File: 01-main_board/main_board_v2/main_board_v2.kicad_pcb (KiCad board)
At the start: 4 copper layers, 96.4 x 65.3 mm, 3 parts, among them J1 Mezzanine Edge, J4 DB44 (Analog | Digital)

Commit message: made progress on layout
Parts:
- added AE1: Antenna_Chip, 22XT_Main:XDCR_2450AT18B100E, F.Cu at (111.2, 143.1)
- added BT1: Battery_Cell, Battery:BatteryHolder_LINX_BAT-HLD-012-SMT, F.Cu at (109.0, 76.5)
- added C1: 1 uF, Capacitor_SMD:C_0402_1005Metric, B.Cu at (99.5, 49.0)
- added C10: 4.7uF, Capacitor_SMD:C_0402_1005Metric, B.Cu at (72.1, 46.4)
- added C11: 10uF, Capacitor_SMD:C_0402_1005Metric, F.Cu at (206.3, 106.7)
- added C12: 0.1uF, Capacitor_SMD:C_0402_1005Metric, F.Cu at (206.3, 108.7)
- added C13: 1uF, Capacitor_SMD:C_0402_1005Metric, F.Cu at (151.5, 162.0)
- added C14: 0.1uF, Capacitor_SMD:C_0402_1005Metric, F.Cu at (151.5, 164.0)
- added C15: 10uF, Capacitor_SMD:C_0402_1005Metric, F.Cu at (151.5, 166.0)
- added C16: 0.1uF, Capacitor_SMD:C_0402_1005Metric, F.Cu at (151.5, 167.9)
- added C17: 0.1uF, Capacitor_SMD:C_0402_1005Metric, F.Cu at (151.5, 169.9)
- added C18: 0.1uF, Capacitor_SMD:C_0402_1005Metric, F.Cu at (151.5, 171.9)
- added C19: 1uF, Capacitor_SMD:C_0402_1005Metric, F.Cu at (151.5, 173.8)
- added C2: 1 uF, Capacitor_SMD:C_0402_1005Metric, B.Cu at (106.0, 49.9)
- added C20: 0.1uF, Capacitor_SMD:C_0402_1005Metric, F.Cu at (154.3, 162.0)
- added C21: 0.1uF, Capacitor_SMD:C_0402_1005Metric, F.Cu at (182.7, 80.2)
- added C22: 0.1uF, Capacitor_SMD:C_0402_1005Metric, F.Cu at (223.7, -5.80)
- added C23: 0.1uF, Capacitor_SMD:C_0402_1005Metric, F.Cu at (223.7, -3.83)
- added C24: 0.1uF, Capacitor_SMD:C_0402_1005Metric, F.Cu at (206.3, 114.6)
- added C25: 1.2pF, Capacitor_SMD:C_0402_1005Metric, F.Cu at (194.5, 76.2)
- added C26: 0.1uF, Capacitor_SMD:C_0402_1005Metric, F.Cu at (112.0, 36.5)
- added C27: 0.1uF, Capacitor_SMD:C_0402_1005Metric, F.Cu at (182.7, 82.1)
- added C28: 0.1uF, Capacitor_SMD:C_0402_1005Metric, F.Cu at (165.8, 101.3)
- added C29: 0.1uF, Capacitor_SMD:C_0402_1005Metric, F.Cu at (70.5, 34.3)
- added C3: 0.1uF, Capacitor_SMD:C_0402_1005Metric, B.Cu at (98.4, 31.2)
- added C30: 0.1uF, Capacitor_SMD:C_0402_1005Metric, F.Cu at (72.0, 34.3)
- added C31: 0.1uF, Capacitor_SMD:C_0402_1005Metric, F.Cu at (70.5, 39.3)
- added C32: 0.1uF, Capacitor_SMD:C_0402_1005Metric, F.Cu at (72.0, 39.3)
- added C33: 0.1uF, Capacitor_SMD:C_0402_1005Metric, F.Cu at (165.8, 103.3)
- added C34: 0.1uF, Capacitor_SMD:C_0402_1005Metric, F.Cu at (165.8, 105.2)
- added C35: 0.1uF, Capacitor_SMD:C_0402_1005Metric, F.Cu at (165.8, 107.2)
- added C36: 4.7uF, Capacitor_SMD:C_0402_1005Metric, B.Cu at (72.1, 44.9)
- added C37: 0.1uF, Capacitor_SMD:C_0402_1005Metric, F.Cu at (165.8, 109.2)
- added C38: 10uF, Capacitor_SMD:C_0402_1005Metric, B.Cu at (85.8, 55.0)
- added C39: 22uF, Capacitor_SMD:C_0402_1005Metric, B.Cu at (84.8, 49.0)
- added C4: 0.1uF, Capacitor_SMD:C_0402_1005Metric, B.Cu at (105.9, 28.7)
- added C40: 0.1uF, Capacitor_SMD:C_0402_1005Metric, F.Cu at (104.0, 38.0)
- added C41: 0.1uF, Capacitor_SMD:C_0402_1005Metric, F.Cu at (193.4, 114.6)
- added C42: 0.1uF, Capacitor_SMD:C_0402_1005Metric, F.Cu at (165.8, 111.2)
- added C43: 0.1uF, Capacitor_SMD:C_0402_1005Metric, F.Cu at (168.7, 99.3)
- added C44: 0.1uF, Capacitor_SMD:C_0402_1005Metric, F.Cu at (168.7, 101.3)
- added C45: 0.1uF, Capacitor_SMD:C_0402_1005Metric, F.Cu at (168.7, 103.3)
- added C46: 0.1uF, Capacitor_SMD:C_0402_1005Metric, F.Cu at (168.7, 105.2)
- added C47: 14pF, Capacitor_SMD:C_0402_1005Metric, F.Cu at (194.5, 78.2)
- added C48: 14pF, Capacitor_SMD:C_0402_1005Metric, F.Cu at (194.5, 80.2)
- added C49: 17pF, Capacitor_SMD:C_0402_1005Metric, F.Cu at (194.5, 82.1)
- added C5: 1.5pF, Capacitor_SMD:C_0603_1608Metric, F.Cu at (188.2, 76.5)
- added C50: 17pF, Capacitor_SMD:C_0402_1005Metric, F.Cu at (194.5, 84.1)
- added C51: 39pF, Capacitor_SMD:C_0402_1005Metric, B.Cu at (108.4, 31.2)
- added C52: 39pF, Capacitor_SMD:C_0402_1005Metric, B.Cu at (108.4, 33.7)
- added C53: 2.2uF, Capacitor_SMD:C_0402_1005Metric, F.Cu at (197.4, 76.2)
- added C54: 2.2uF, Capacitor_SMD:C_0402_1005Metric, F.Cu at (197.4, 78.2)
- added C55: 0.1uF, Capacitor_SMD:C_0402_1005Metric, F.Cu at (197.4, 80.2)
- added C56: 0.1uF, Capacitor_SMD:C_0402_1005Metric, F.Cu at (197.4, 82.1)
- added C57: 2.2uF, Capacitor_SMD:C_0402_1005Metric, F.Cu at (197.4, 84.1)
- added C58: 0.1uF, Capacitor_SMD:C_0402_1005Metric, F.Cu at (200.2, 76.2)
- added C59: 10nF, Capacitor_SMD:C_0402_1005Metric, F.Cu at (200.2, 78.2)
- added C6: 1.5pF, Capacitor_SMD:C_0603_1608Metric, F.Cu at (188.2, 79.0)
- added C60: 0.1uF, Capacitor_SMD:C_0402_1005Metric, F.Cu at (200.2, 80.2)
- added C62: 0.1uF, Capacitor_SMD:C_0603_1608Metric, F.Cu at (188.2, 81.5)
- added C7: 2.2uF, Capacitor_SMD:C_0402_1005Metric, F.Cu at (53.5, 52.0)
- added C8: 0.1uF, Capacitor_SMD:C_0402_1005Metric, B.Cu at (72.2, 47.9)
- added C9: 0.1uF, Capacitor_SMD:C_0402_1005Metric, B.Cu at (74.7, 47.9)
- added D1: D_Schottky, 22XT_Main:DO-214BA_MCH, B.Cu at (172.0, 48.0)
- added D2: RCLAMP3354S.TCT, Package_TO_SOT_SMD:SOT-23-5, B.Cu at (51.1, 38.8)
- added IC1: MAX6105EUR+T, Package_TO_SOT_SMD:SOT-23-3, F.Cu at (197.4, 107.9)
- added IC10: ESP32-S3, 22XT_Main:QFN40P700X700X90-57N-D, F.Cu at (105.0, 136.8)
- added IC11: TPS62173DSGT, 22XT_Main:SON50P200X200X80-9N, B.Cu at (85.6, 52.0)
- added IC2: LP5907MFX-2.5_NOPB, Package_TO_SOT_SMD:SOT-23-5, B.Cu at (102.6, 49.5)
- added IC3: TS3USB30EDGSR, 22XT_Main:SOP50P490X110-10N, F.Cu at (104.1, 143.8)
- added IC4: SPX3819S-L_TR, 22XT_Main:SOIC127P600X175-8N, F.Cu at (58.5, 51.5)
- added IC5: INA827AIDGK, 22XT_Main:SOP65P490X110-8N, F.Cu at (118.3, 52.7)
- added IC6: AD7175-8BCPZ-RL7, 22XT_Main:QFN50P600X600X80-41N-D, F.Cu at (117.5, 25.5)
- added IC7: INA827AIDGK, 22XT_Main:SOP65P490X110-8N, F.Cu at (118.3, 57.3)
- added IC8: AD8591ARTZ-REEL7, 22XT_Main:SOT95P280X145-6N, F.Cu at (59.2, 128.0)
- added IC9: LSF0108PWR, 22XT_Main:SOP65P640X120-20N, F.Cu at (109.0, 41.0)
- added L1: 2.2uH, Inductor_SMD:L_0402_1005Metric, B.Cu at (87.8, 49.0)
- added L2: 2.7nH, Inductor_SMD:L_0603_1608Metric, F.Cu at (188.2, 84.0)
- added L3: 2.7nH, Inductor_SMD:L_0402_1005Metric, F.Cu at (191.6, 76.2)
- added L4: 3.3nH, Inductor_SMD:L_0402_1005Metric, F.Cu at (191.6, 78.2)
- added L5: 2nH, Inductor_SMD:L_0402_1005Metric, F.Cu at (191.6, 80.2)
- added NT1: NetTie_4_Cross, NetTie:NetTie-4_SMD_Pad0.5mm, F.Cu at (203.3, 90.0)
- added NT2: NetTie_3_Tee, NetTie:NetTie-2_SMD_Pad0.5mm, F.Cu at (203.3, 88.0)
- added R1: 10k, Resistor_SMD:R_0402_1005Metric, F.Cu at (160.1, 162.0)
- added R10: 36.5k, Resistor_SMD:R_0402_1005Metric, B.Cu at (56.0, 52.5)
- added R100: 10k, Resistor_SMD:R_0402_1005Metric, F.Cu at (191.6, 82.2)
- added R101: 10k, Resistor_SMD:R_0402_1005Metric, F.Cu at (191.6, 84.2)
- added R11: 100k, Resistor_SMD:R_0402_1005Metric, B.Cu at (88.5, 51.2)
- added R12: 64.2k (0.1%), Resistor_SMD:R_0402_1005Metric, F.Cu at (220.8, -9.73)
- added R13: 100R, Resistor_SMD:R_0402_1005Metric, F.Cu at (160.1, 166.0)
- added R14: DNP, Resistor_SMD:R_0402_1005Metric, F.Cu at (171.4, 92.8)
- added R15: DNP, Resistor_SMD:R_0402_1005Metric, F.Cu at (113.5, 32.5)
- added R16: DNP, Resistor_SMD:R_0402_1005Metric, F.Cu at (115.6, 45.5)
- added R17: DNP, Resistor_SMD:R_0402_1005Metric, F.Cu at (118.5, 32.5)
- added R18: DNP, Resistor_SMD:R_0402_1005Metric, F.Cu at (118.5, 35.5)
- added R19: DNP, Resistor_SMD:R_0402_1005Metric, F.Cu at (118.5, 37.5)
- added R2: DNP, Resistor_SMD:R_0402_1005Metric, F.Cu at (171.4, 90.8)
- added R20: 352R (0.1%), Resistor_SMD:R_0402_1005Metric, F.Cu at (220.8, -7.75)
- added R21: 352R (0.1%), Resistor_SMD:R_0402_1005Metric, F.Cu at (220.8, -5.75)
- added R22: 352R (0.1%), Resistor_SMD:R_0402_1005Metric, F.Cu at (220.8, -3.77)
- added R24: 352R (0.1%), Resistor_SMD:R_0402_1005Metric, F.Cu at (220.8, -1.77)
- added R25: 64.2k (0.1%), Resistor_SMD:R_0402_1005Metric, F.Cu at (220.8, 0.21)
- added R26: DNP, Resistor_SMD:R_0402_1005Metric, F.Cu at (121.5, 44.5)
- added R27: 52.3R, Resistor_SMD:R_0402_1005Metric, B.Cu at (71.0, 35.8)
- added R28: 52.3R, Resistor_SMD:R_0402_1005Metric, B.Cu at (71.0, 37.8)
- added R29: DNP, Resistor_SMD:R_0402_1005Metric, F.Cu at (120.0, 44.5)
- added R3: 1.69k, Resistor_SMD:R_0402_1005Metric, B.Cu at (110.0, 39.0)
- added R30: DNP, Resistor_SMD:R_0402_1005Metric, F.Cu at (121.4, 33.5)
- added R31: DNP, Resistor_SMD:R_0402_1005Metric, F.Cu at (121.4, 35.5)
- added R32: DNP, Resistor_SMD:R_0402_1005Metric, F.Cu at (121.4, 37.5)
- added R33: 20R, Resistor_SMD:R_0402_1005Metric, F.Cu at (171.4, 94.8)
- added R34: DNP, Resistor_SMD:R_0402_1005Metric, F.Cu at (121.4, 39.5)
- added R38: 352R (0.1%), Resistor_SMD:R_0402_1005Metric, F.Cu at (220.8, 2.21)
- added R39: 352R (0.1%), Resistor_SMD:R_0402_1005Metric, F.Cu at (220.8, 4.20)
- added R4: DNP, Resistor_SMD:R_0402_1005Metric, F.Cu at (115.1, 32.5)
- added R40: 200k, Resistor_SMD:R_0402_1005Metric, B.Cu at (109.5, 36.5)
- added R41: 1.6k, Resistor_SMD:R_0402_1005Metric, F.Cu at (171.6, 105.3)
- added R42: 1.6k, Resistor_SMD:R_0402_1005Metric, F.Cu at (171.6, 107.3)
- added R43: 1.6k, Resistor_SMD:R_0402_1005Metric, F.Cu at (174.5, 99.3)
- added R44: 1.6k, Resistor_SMD:R_0402_1005Metric, F.Cu at (174.5, 101.3)
- added R45: 22k, Resistor_SMD:R_0402_1005Metric, B.Cu at (53.5, 54.0)
- added R46: 1.6k, Resistor_SMD:R_0402_1005Metric, F.Cu at (174.5, 103.3)
- added R47: 400R, Resistor_SMD:R_0402_1005Metric, B.Cu at (72.8, 58.6)
- added R48: 1.6k, Resistor_SMD:R_0402_1005Metric, F.Cu at (174.5, 105.3)
- added R49: 1.6k, Resistor_SMD:R_0402_1005Metric, F.Cu at (174.5, 107.3)
- added R5: 680R, Resistor_SMD:R_0402_1005Metric, F.Cu at (160.1, 164.0)
- added R50: 120, Resistor_SMD:R_1206_3216Metric, F.Cu at (103.5, 23.5)
- added R6: 1.07k, Resistor_SMD:R_0402_1005Metric, B.Cu at (108.0, 41.5)
- added R60: 100k, Resistor_SMD:R_0402_1005Metric, B.Cu at (76.8, 51.6)
- added R63: 1.6k, Resistor_SMD:R_0402_1005Metric, F.Cu at (177.4, 99.3)
- added R64: 1.6k, Resistor_SMD:R_0402_1005Metric, F.Cu at (177.4, 101.3)
- added R65: 1.6k, Resistor_SMD:R_0402_1005Metric, F.Cu at (177.4, 103.3)
- added R7: 1.07k, Resistor_SMD:R_0402_1005Metric, B.Cu at (108.0, 39.0)
- added R8: 1.69k, Resistor_SMD:R_0402_1005Metric, B.Cu at (110.0, 41.5)
- added T1: 749013011, 22XT_Main:749013011, F.Cu at (62.6, 36.9)
- added TP1: MISO_ESP, TestPoint:TestPoint_Pad_1.0x1.0mm, F.Cu at (203.2, 76.8)
- added TP10: 3V3_teensy TP, TestPoint:TestPoint_Pad_1.0x1.0mm, F.Cu at (174.4, 94.6)
- added TP11: 5V_buck, TestPoint:TestPoint_Pad_1.0x1.0mm, B.Cu at (89.5, 54.5)
- added TP12: 5V_usb, TestPoint:TestPoint_Pad_1.0x1.0mm, F.Cu at (48.5, 45.0)
- added TP13: 5V_ref, TestPoint:TestPoint_Pad_1.0x1.0mm, F.Cu at (196.7, 120.1)
- added TP2: MOSI_ESP, TestPoint:TestPoint_Pad_1.0x1.0mm, F.Cu at (203.2, 79.8)
- added TP3: SCLK_ESP, TestPoint:TestPoint_Pad_1.0x1.0mm, F.Cu at (203.2, 82.8)
- added TP4: MISO1, TestPoint:TestPoint_Pad_1.0x1.0mm, F.Cu at (160.2, 172.5)
- added TP5: MOSI1, TestPoint:TestPoint_Pad_1.0x1.0mm, F.Cu at (160.2, 175.6)
- added TP6: SCLK1, TestPoint:TestPoint_Pad_1.0x1.0mm, F.Cu at (160.2, 178.6)
- added TP7: 5V TP, TestPoint:TestPoint_Pad_1.0x1.0mm, B.Cu at (69.0, 53.0)
- added TP8: 3V3 TP, TestPoint:TestPoint_Pad_1.0x1.0mm, F.Cu at (56.5, 57.0)
- added TP9: 2V5 TP, TestPoint:TestPoint_Pad_1.0x1.0mm, F.Cu at (102.1, 45.5)
- added U1: Teensy4.1, 22XT_Main:Teensy41, F.Cu at (87.8, 52.7)
- added U2: AD5689RARUZ-RL7, 22XT_Main:RU_16_ADI, F.Cu at (93.8, 135.6)
- added U3: MCP2562FD-E/SN, Package_SO:SOIC-8_3.9x4.9mm_P1.27mm, B.Cu at (103.5, 32.5)
- added U4: TPS2115APWR, 22XT_Main:SOP65P640X120-8N, B.Cu at (73.2, 52.9)
- added Y1: ECS-400-10-37B2-CKY-TR, 22XT_Main:XTAL_ECS-400-10-37B2-CKY-TR, F.Cu at (111.6, 137.3)
- added Y2: ECS-.327-12.5-34B-TR, 22XT_Main:XTAL_ECS-.327-12.5-34B-TR, F.Cu at (112.3, 133.9)
- moved J1 14.8 mm to (41.5, 31.8)
- moved G*** 0.87 mm to (44.7, 24.9)
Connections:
- J1 pad 3: unconnected-(J1-Pin_3-Pad3) -> usb_mux_s
- J4 pad 1: unconnected-(J4-Pin_1-Pad1) -> 3V3_out
- J4 pad 10: AN5 -> AN4
- J4 pad 11: AN4 -> AN3
- J4 pad 12: AN3 -> AN2
- J4 pad 13: AN2 -> AN1
- J4 pad 14: AN1 -> sg_sense_1_FL
- J4 pad 15: GP/Int1 -> sg_sense_2_FR
- J4 pad 16: B- -> CANH
- J4 pad 17: 11.1V_battery -> CANL
- J4 pad 18: sg2+ -> GP/Int2
- J4 pad 19: sg_sense_2_FR -> GP/Int1
- J4 pad 2: 5V_buck_PG -> GNDA
- J4 pad 20: sg1+ -> DN6
- J4 pad 21: DN6 -> DN5
- J4 pad 22: DN5 -> DN4
- J4 pad 23: DN4 -> 11.1V_battery
- J4 pad 24: SDA_mag -> AN10
- J4 pad 25: AN10 -> AN9
- J4 pad 26: AN9 -> AN8
- J4 pad 27: AN8 -> AN7
- J4 pad 28: AN7 -> AN6
- J4 pad 29: AN6 -> sg1+
- J4 pad 3: unconnected-(J4-Pin_3-Pad3) -> SCL_mag
- J4 pad 30: GP/Int2 -> sg2+
- J4 pad 31: B- -> GNDD
- J4 pad 32: 11.1V_battery -> GNDD
- J4 pad 33: unconnected-(J4-Pin_33-Pad33) -> GNDD
- J4 pad 34: sg_sense_1_FL -> GNDD
- J4 pad 35: unconnected-(J4-Pin_35-Pad35) -> 5V
- J4 pad 36: GNDD -> 5V
- J4 pad 37: GNDD -> B-
- J4 pad 38: 3V3_out -> 5V_ref
- J4 pad 39: CANL -> GNDA
- J4 pad 4: 2V5 -> SDA_mag
- J4 pad 40: CANH -> GNDA
- J4 pad 43: 5V -> 2V5
- J4 pad 44: 5V -> 2V5
- J4 pad 5: 2V5 -> DN3
- J4 pad 6: DN3 -> DN2
- J4 pad 7: DN2 -> DN1
- J4 pad 8: DN1 -> 11.1V_battery
- J4 pad 9: SCL_mag -> AN5
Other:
- outline, holes or cut-outs redrawn

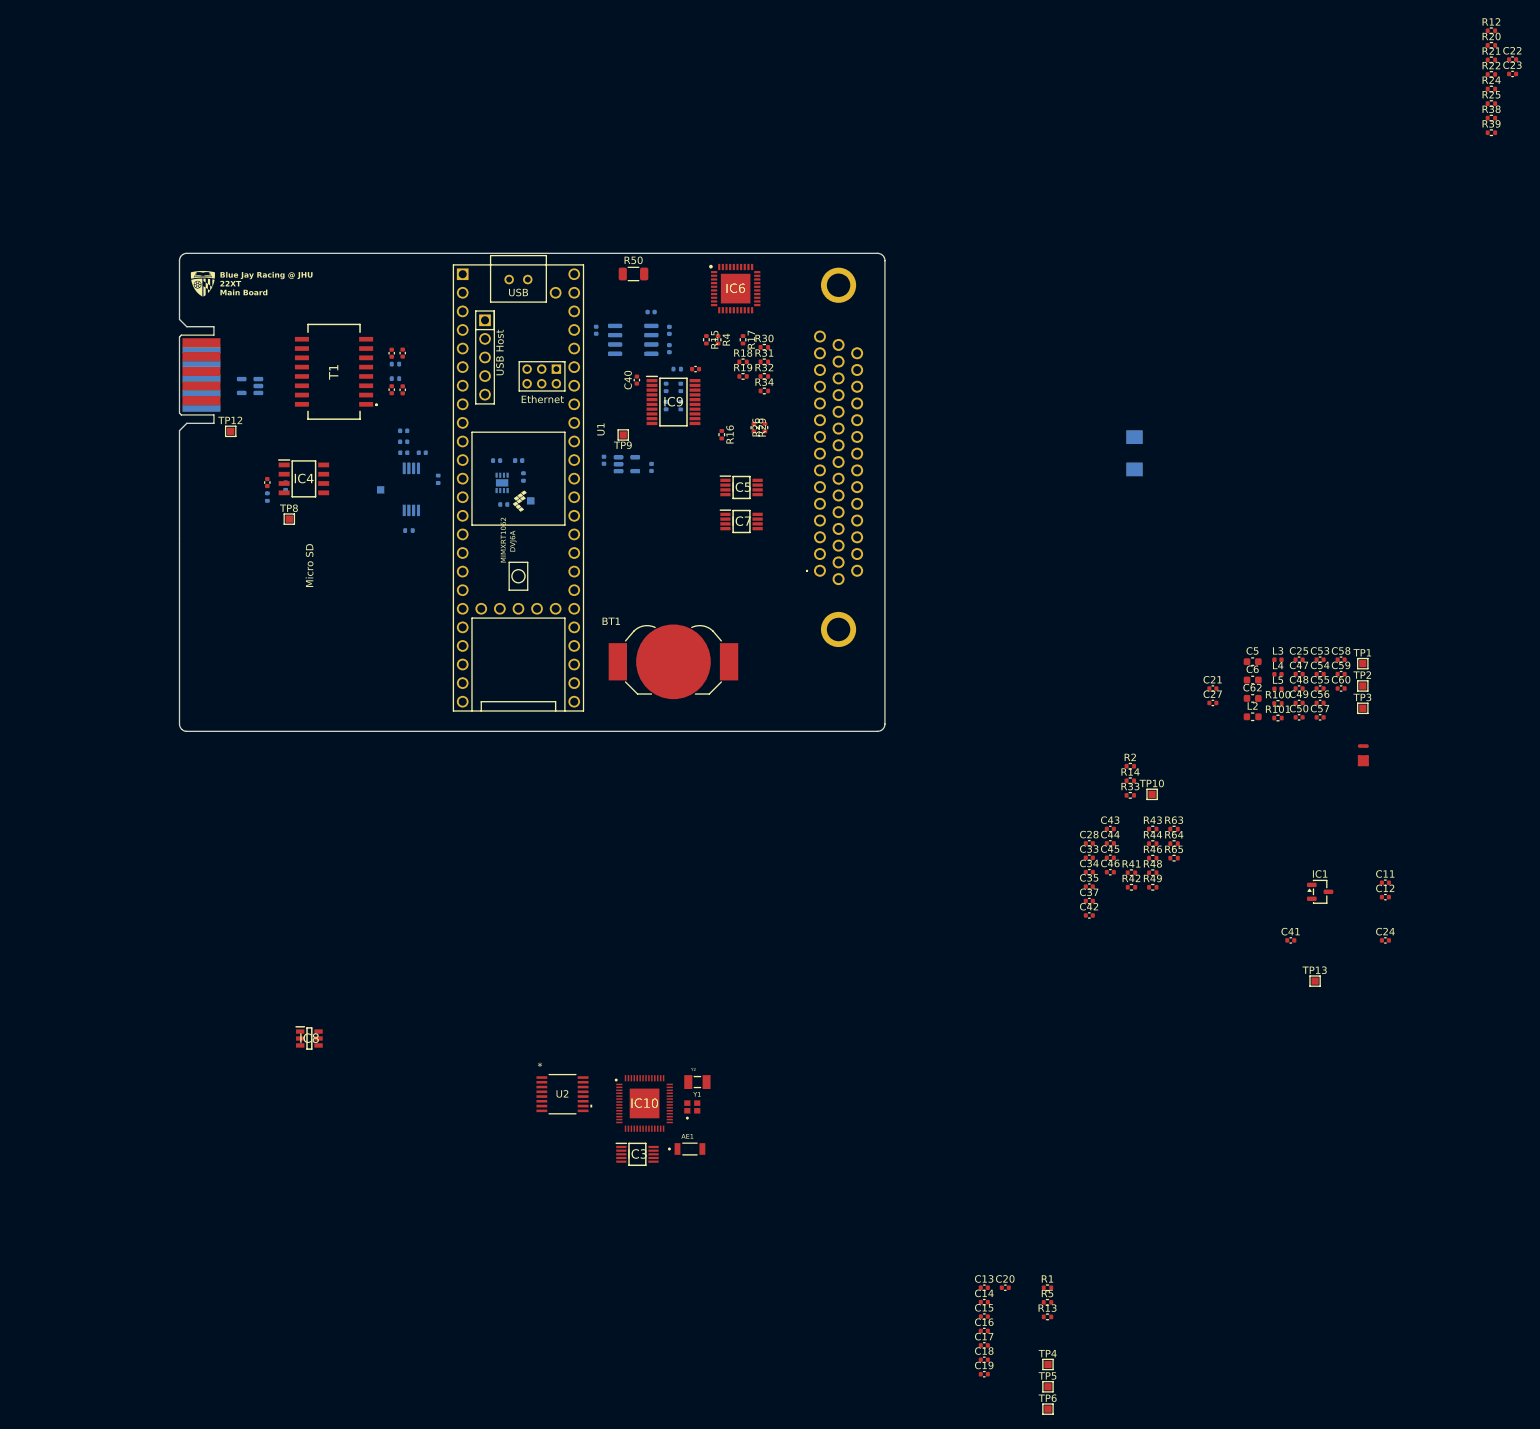
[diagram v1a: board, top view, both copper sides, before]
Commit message: changed buck converter, finished ground + power plane layout
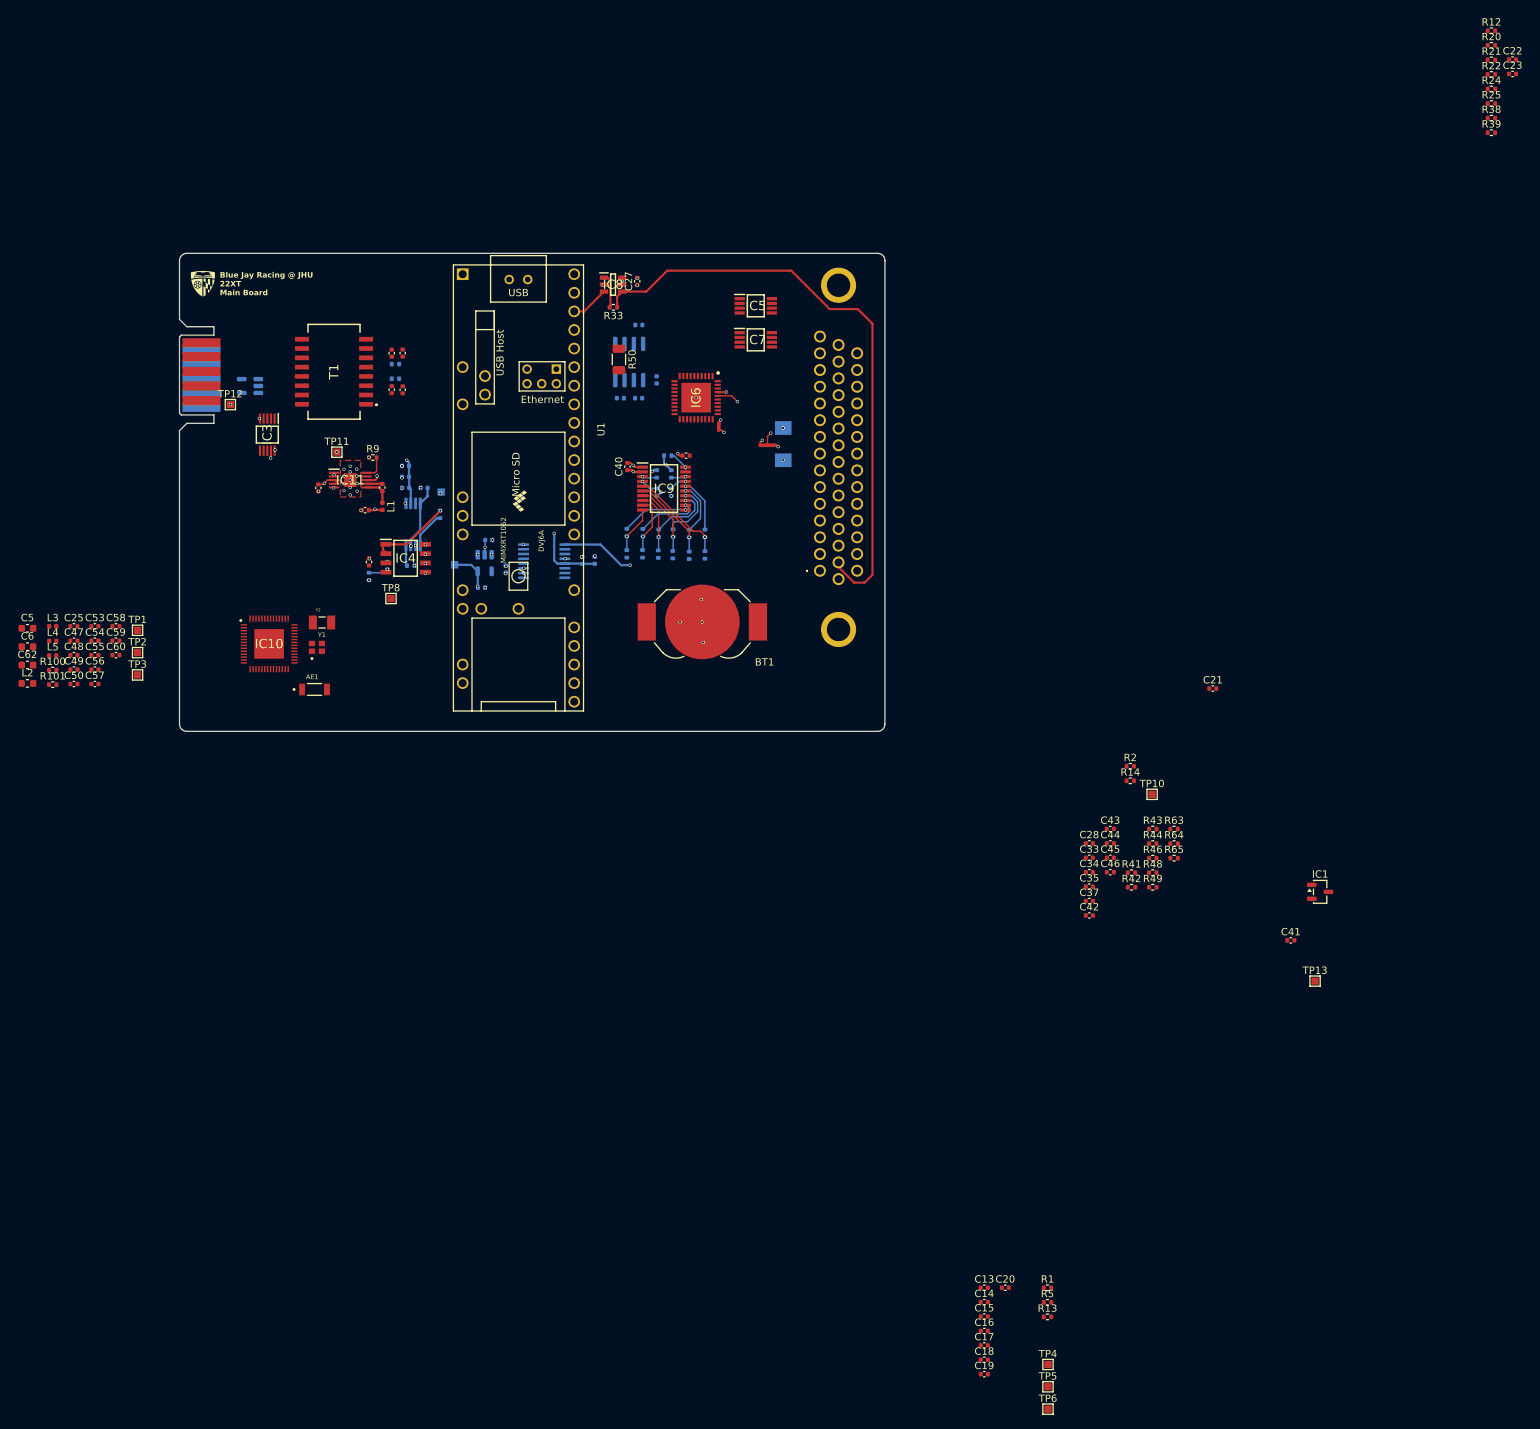
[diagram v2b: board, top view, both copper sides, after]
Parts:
- removed R11: 100k, Resistor_SMD:R_0402_1005Metric
- added C61: 22uF, Capacitor_SMD:C_0402_1005Metric, F.Cu at (66.9, 55.8)
- added R9: 215k, Resistor_SMD:R_0402_1005Metric, F.Cu at (67.9, 48.6)
- C11, C12, C24, R15, R16, R17, R18, R19, R26, R29, R30, R31, R32, R34, R4, TP9, U2: moved to B.Cu
- C38: value 10uF -> 0.47uF; moved to F.Cu
- C39: value 22uF -> 4.7uF; moved to F.Cu
- C51, C52: value 39pF -> 40pF
- IC11: value TPS62173DSGT -> LT3973EMSE-5#PBF; footprint 22XT_Main:SON50P200X200X80-9N -> 22XT_Main:SOP50P490X110-11N; moved to F.Cu
- L1: value 2.2uH -> 15uH; moved to F.Cu
- NT1: value NetTie_4_Cross -> NetTie_2; footprint NetTie:NetTie-4_SMD_Pad0.5mm -> NetTie:NetTie-2_SMD_Pad0.5mm
- NT2: footprint NetTie:NetTie-2_SMD_Pad0.5mm -> NetTie:NetTie-3_SMD_Pad0.5mm
- TP11: moved to F.Cu
- moved C25 167.5 mm to (27.1, 71.7)
- moved C47 167.5 mm to (27.1, 73.6)
- moved C48 167.5 mm to (27.1, 75.6)
- moved C49 167.5 mm to (27.1, 77.6)
- moved C5 167.5 mm to (20.7, 71.9)
- moved C50 167.5 mm to (27.1, 79.5)
- moved C53 167.5 mm to (29.9, 71.7)
- moved C54 167.5 mm to (29.9, 73.6)
- moved C55 167.5 mm to (29.9, 75.6)
- moved C56 167.5 mm to (29.9, 77.6)
- moved C57 167.5 mm to (29.9, 79.5)
- moved C58 167.5 mm to (32.8, 71.7)
- moved C59 167.5 mm to (32.8, 73.6)
- moved C6 167.5 mm to (20.7, 74.4)
- moved C60 167.5 mm to (32.8, 75.6)
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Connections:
- BT1 pad 2: GNDA -> PGND
- C38 pad 1: PGND -> Net-(IC11-BOOST)
- C38 pad 2: 11.1V -> Net-(IC11-SW)
- C39 pad 1: 5V_buck -> 11.1V
- C39 pad 2: GNDA -> PGND
- C7 pad 1: GNDD -> PGND
- IC11 pad 1: PGND -> 5V_buck
- IC11 pad 2: 11.1V -> 5V_buck
- IC11 pad 4: GNDA -> 11.1V
- IC11 pad 5: GNDA -> PGND
- IC11 pad 6: 5V_buck -> Net-(IC11-SW)
- IC11 pad 7: Net-(IC11-SW) -> Net-(IC11-BOOST)
- IC11 pad 8: 5V_buck_PG -> 5V_buck
- IC4 pad 5: GNDD -> PGND
- IC4 pad 6: GNDD -> PGND
- IC4 pad 7: GNDD -> PGND
- IC4 pad 8: GNDD -> PGND
- J4 pad 1: 3V3_out -> CANH
- J4 pad 16: CANH -> unconnected-(J4-Pin_16-Pad16)
- J4 pad 17: CANL -> 3V3_out
- J4 pad 2: GNDA -> CANL
- NT1 pad 2: B- -> GNDD
- NT2 pad 1: GNDA -> PGND
- NT2 pad 2: GNDD -> B-
- R14 pad 2: Net-(U1-17_A3_TX4_SDA1) -> Net-(U1-35_TX8)
- R2 pad 2: Net-(U1-16_A2_RX4_SCL1) -> Net-(U1-34_RX8)
- R45 pad 2: GNDD -> PGND
- U1 pad 26: unconnected-(U1-34_RX8-Pad26) -> Net-(U1-34_RX8)
- U1 pad 27: unconnected-(U1-35_TX8-Pad27) -> Net-(U1-35_TX8)
- U1 pad 36: D1_shift -> D6_shift
- U1 pad 37: D2_shift -> D5_shift
- U1 pad 38: Net-(U1-16_A2_RX4_SCL1) -> D4_shift
- U1 pad 39: Net-(U1-17_A3_TX4_SDA1) -> D3_shift
- U1 pad 42: D3_shift -> D2_shift
- U1 pad 43: D4_shift -> D1_shift
- U1 pad 6: unconnected-(U1-4_BCLK2-Pad6) -> usb_mux_s
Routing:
- net 3V3_out: track 0.00 -> 81.7 mm
- net 2V5_ref: track 0.00 -> 42.9 mm, vias 0 -> 2
- net 5V: track 0.00 -> 28.7 mm, vias 0 -> 9
- net D1_shift: track 0.00 -> 13.5 mm, vias 0 -> 1
- net D2_shift: track 0.00 -> 11.4 mm, vias 0 -> 1
- net 5V_buck: track 0.00 -> 9.96 mm, vias 0 -> 5
- net D3_shift: track 0.00 -> 9.84 mm, vias 0 -> 1
- net DN6: track 0.00 -> 9.13 mm, vias 0 -> 1
- net 5V_usb: track 0.00 -> 9.06 mm, vias 0 -> 3
- net 2V5: track 0.00 -> 8.79 mm, vias 0 -> 2
- net DN5: track 0.00 -> 8.48 mm, vias 0 -> 1
- net DN4: track 0.00 -> 8.39 mm, vias 0 -> 1
- net D4_shift: track 0.00 -> 8.31 mm, vias 0 -> 1
- net DN3: track 0.00 -> 8.15 mm, vias 0 -> 1
- net D5_shift: track 0.00 -> 7.77 mm, vias 0 -> 1
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- added copper zone on In2.Cu, net 11.1V
- added copper zone on In2.Cu, net 11.1V_battery
- added copper zone on In2.Cu, net 2V5
- added copper zone on In2.Cu, net 3V3
- added copper zone on In2.Cu, net 3V3_teensy
- added copper zone on In2.Cu, net 5V
- added copper zone on In2.Cu, net 5V_buck
- added copper zone on In2.Cu, net 5V_usb
- added copper zone on In1.Cu, net B-
- added copper zone on In1.Cu, net GNDA
- added copper zone on In1.Cu, net GNDD
- added copper zone on F.Cu, net PGND
- added copper zone on In1.Cu, net PGND
